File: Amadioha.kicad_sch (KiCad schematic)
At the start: 70 parts, among them IC1 ACS37800KMACTR-030B3-I2C, J1 691137710002, J2 SW_Debug, J3 691137710002, K1 G6DN-1A-SL_DC5, Q1 BSS138, Q2 BSS138, Q3 BSS138, SW1 PTS815, U1 STM32WB55CGU6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

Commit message: PCB validation and manufacturing
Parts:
- added C21: 0u1, Capacitor_SMD:C_0603_1608Metric_Pad1.08x0.95mm_HandSolder, symbol Device:C
- added SW2: PTS815, PS815_SJK:PTS815SJK250SMTRLFS, symbol Switch:SW_MEC_5E
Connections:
- net GND: now also C21.1, SW2.1, SW2.2
- net Pair: now reaches U1.42 (PA15)
- net Pair: now also C21.2, SW2.3 (K), SW2.4 (A)
- no-connect marks 21 -> 20

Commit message: BOM
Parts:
- J2: now in the parts list
- L1: now not fitted
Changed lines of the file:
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@@
 		(unit 1)
 		(exclude_from_sim no)
-		(in_bom no)
+		(in_bom yes)
 		(on_board yes)
 		(dnp no)
@@
 		(in_bom yes)
 		(on_board yes)
-		(dnp no)
+		(dnp yes)
 		(fields_autoplaced yes)
 		(property "Reference" "L1"

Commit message: revision norm.
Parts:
- L1: now fitted
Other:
- note added: "${TITLE} ${REVISION}"
- title: Amadiaoha - Reloaded -> Amadiaoha
- moved on the sheet: H1, H2, H3, Q2, Q3, R10, R11, R12, R13

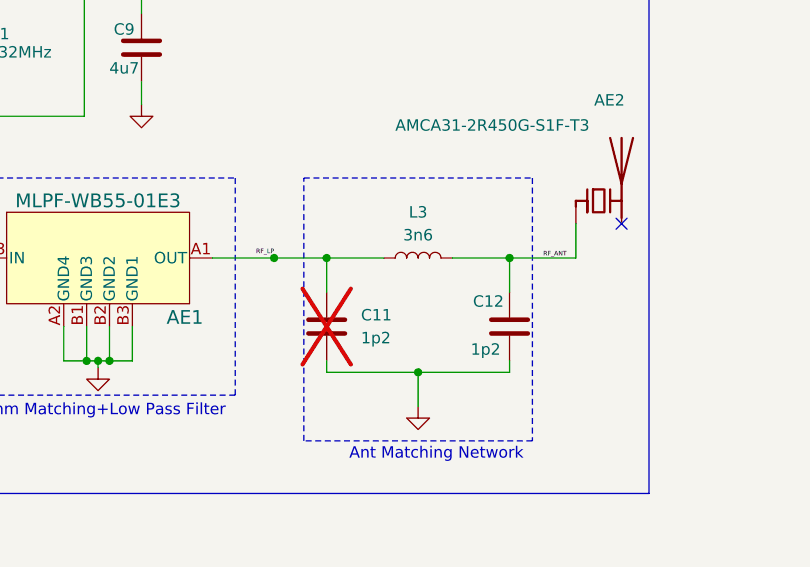
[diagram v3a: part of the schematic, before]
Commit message: trace width ajdustment
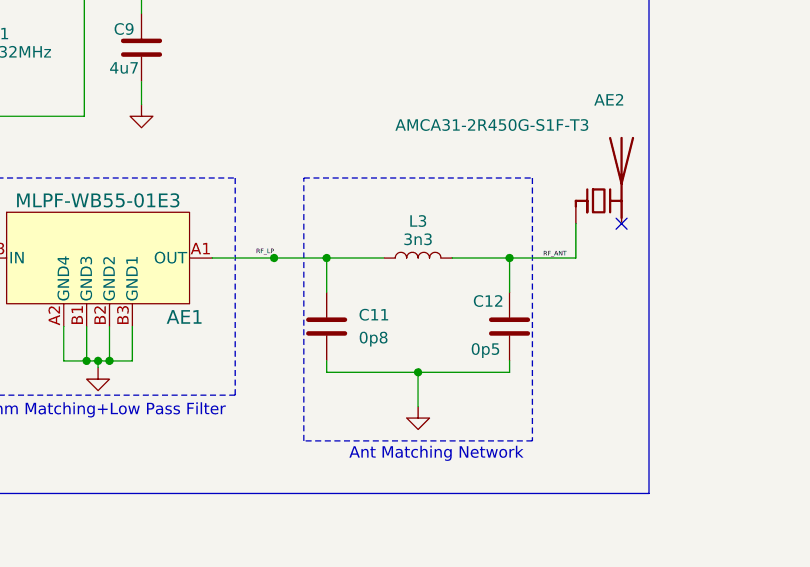
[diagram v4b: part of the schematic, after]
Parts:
- C11: value 1p2 -> 0p8; now fitted
- C12: value 1p2 -> 0p5
- L3: value 3n6 -> 3n3
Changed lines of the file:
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@@
 		(in_bom yes)
 		(on_board yes)
-		(dnp yes)
+		(dnp no)
 		(fields_autoplaced yes)
 		(property "Reference" "C11"
-			(at 251.714 145.5419 0)
+			(at 251.46 145.5419 0)
 			(effects
 				(font
@@
 			)
 		)
-		(property "Value" "1p2"
-			(at 251.714 148.0819 0)
+		(property "Value" "0p8"
+			(at 251.46 148.0819 0)
 			(effects
 				(font
@@
 		(on_board yes)
 		(dnp no)
-		(fields_autoplaced yes)
 		(property "Reference" "L3"
-			(at 258.064 134.112 90)
-			(effects
-				(font
-					(size 1.27 1.27)
-				)
-			)
-		)
-		(property "Value" "3n6"
-			(at 258.064 136.652 90)
+			(at 258.064 135.128 90)
+			(effects
+				(font
+					(size 1.27 1.27)
+				)
+			)
+		)
+		(property "Value" "3n3"
+			(at 258.064 137.16 90)
 			(effects
 				(font
@@
 			)
 		)
-		(property "Value" "1p2"
+		(property "Value" "0p5"
 			(at 263.906 149.352 0)
 			(effects

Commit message: 1/7/2026
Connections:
- net GND: now also C9.1; no longer C9.2
- net SMPSFB: now also C9.2; no longer C9.1
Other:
- moved on the sheet: C9
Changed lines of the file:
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@@
 	(symbol
 		(lib_id "Device:C")
-		(at 227.33 115.824 0)
-		(mirror y)
+		(at 227.33 115.824 180)
 		(unit 1)
 		(exclude_from_sim no)
@@
 		(dnp no)
 		(property "Reference" "C9"
-			(at 226.568 113.792 0)
+			(at 226.568 117.856 0)
 			(effects
 				(font
@@
 		)
 		(property "Value" "4u7"
-			(at 227.076 118.11 0)
+			(at 227.076 113.538 0)
 			(effects
 				(font
@@
 		)
 		(property "Footprint" "Capacitor_SMD:C_0603_1608Metric"
-			(at 226.3648 119.634 0)
+			(at 226.3648 112.014 0)
 			(effects
 				(font
